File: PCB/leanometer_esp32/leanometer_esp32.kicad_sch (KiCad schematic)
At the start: 32 parts, among them J1 DM3AT-SF-PEJM5, J2 MPU6050, J3 PROG, J4 VBAT, SW1 SW_MEC_5E, SW2 IO0, SW3 EN, U1 ESP32-WROOM-32D, U2 LD1117S33TR_SOT223

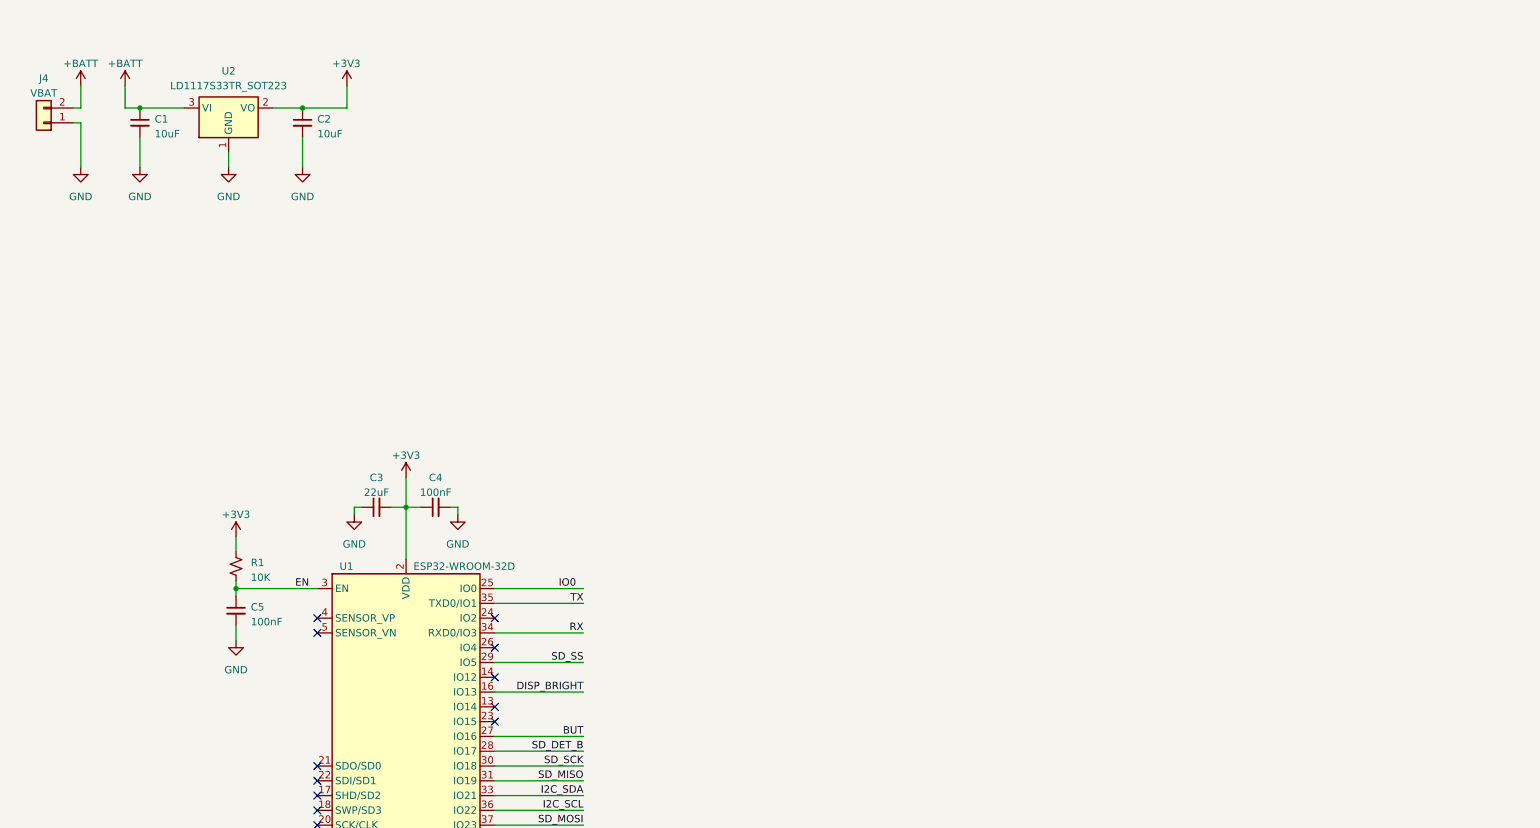
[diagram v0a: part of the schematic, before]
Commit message: Added MPU6050 group
Signed-off-by: theloukou
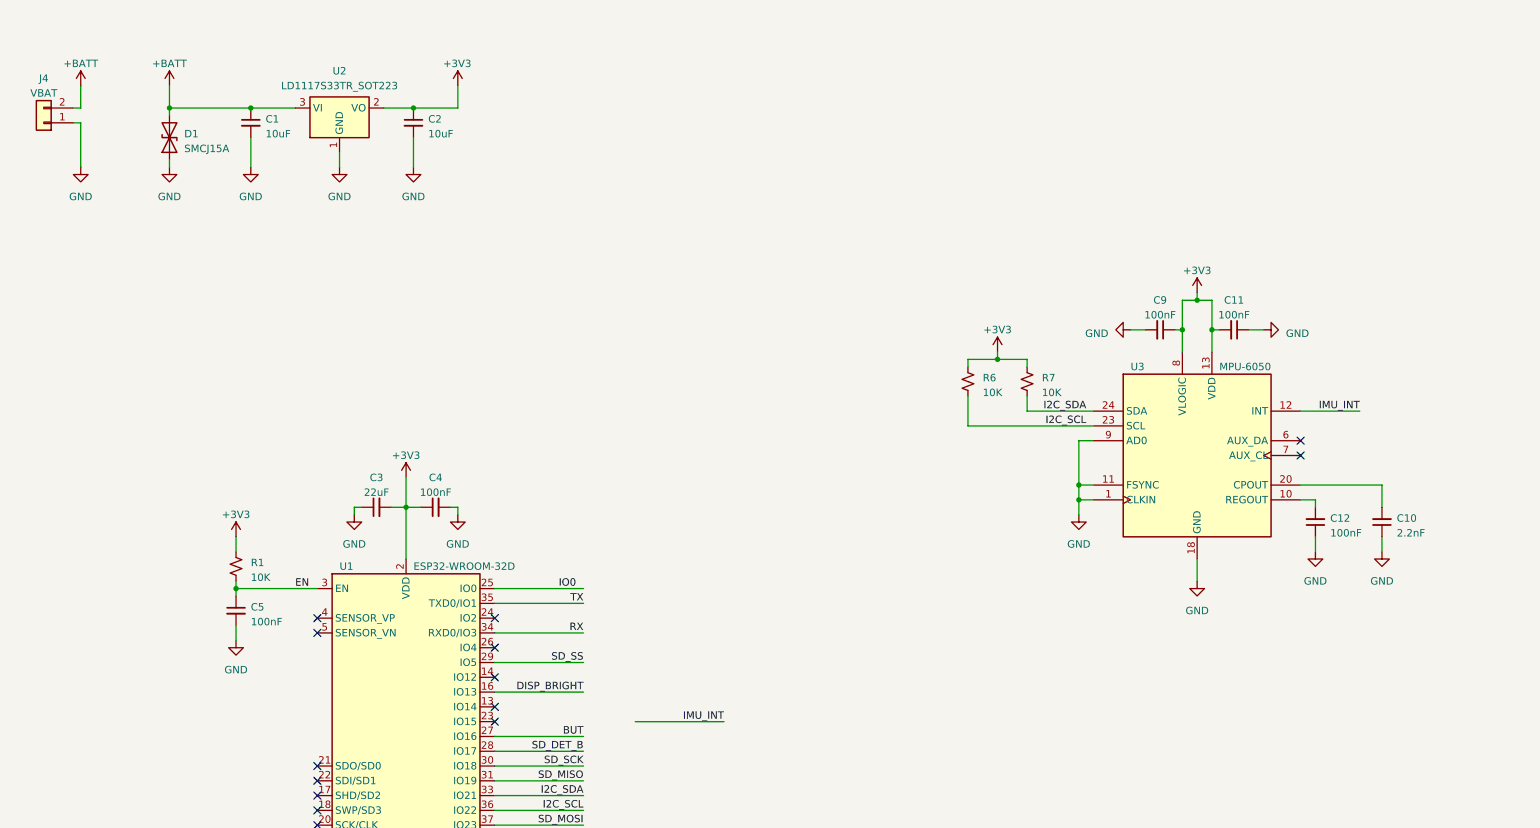
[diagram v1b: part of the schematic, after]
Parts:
- added C10: 2.2nF, symbol Device:C_Small
- added C11, C12, C9: 100nF, symbol Device:C_Small
- added D1: SMCJ15A, Diode_SMD:D_SMC, symbol Device:D_TVS
- added R6, R7: 10K, symbol Device:R_Small_US
- added U3: MPU-6050, Sensor_Motion:InvenSense_QFN-24_4x4mm_P0.5mm, symbol Sensor_Motion:MPU-6050
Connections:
- net +3V3: now also C11.2, C9.1, R6.1, R7.1, U3.13 (VDD), U3.8 (VLOGIC)
- net +BATT: now also D1.2 (A2)
- net GND: now also C10.1, C11.1, C12.1, C9.2, D1.1 (A1), U3.1 (CLKIN), U3.11 (FSYNC), U3.18 (GND), U3.9 (AD0)
- net I2C_SCL: now also R6.2, U3.23 (SCL)
- net I2C_SDA: now also R7.2, U3.24 (SDA)
- new net: C10.2, U3.20 (CPOUT)
- new net: C12.2, U3.10 (REGOUT)
- new net IMU_INT: U3.12 (INT)
- no-connect marks 15 -> 17
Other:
- moved on the sheet: C1, C2, U2

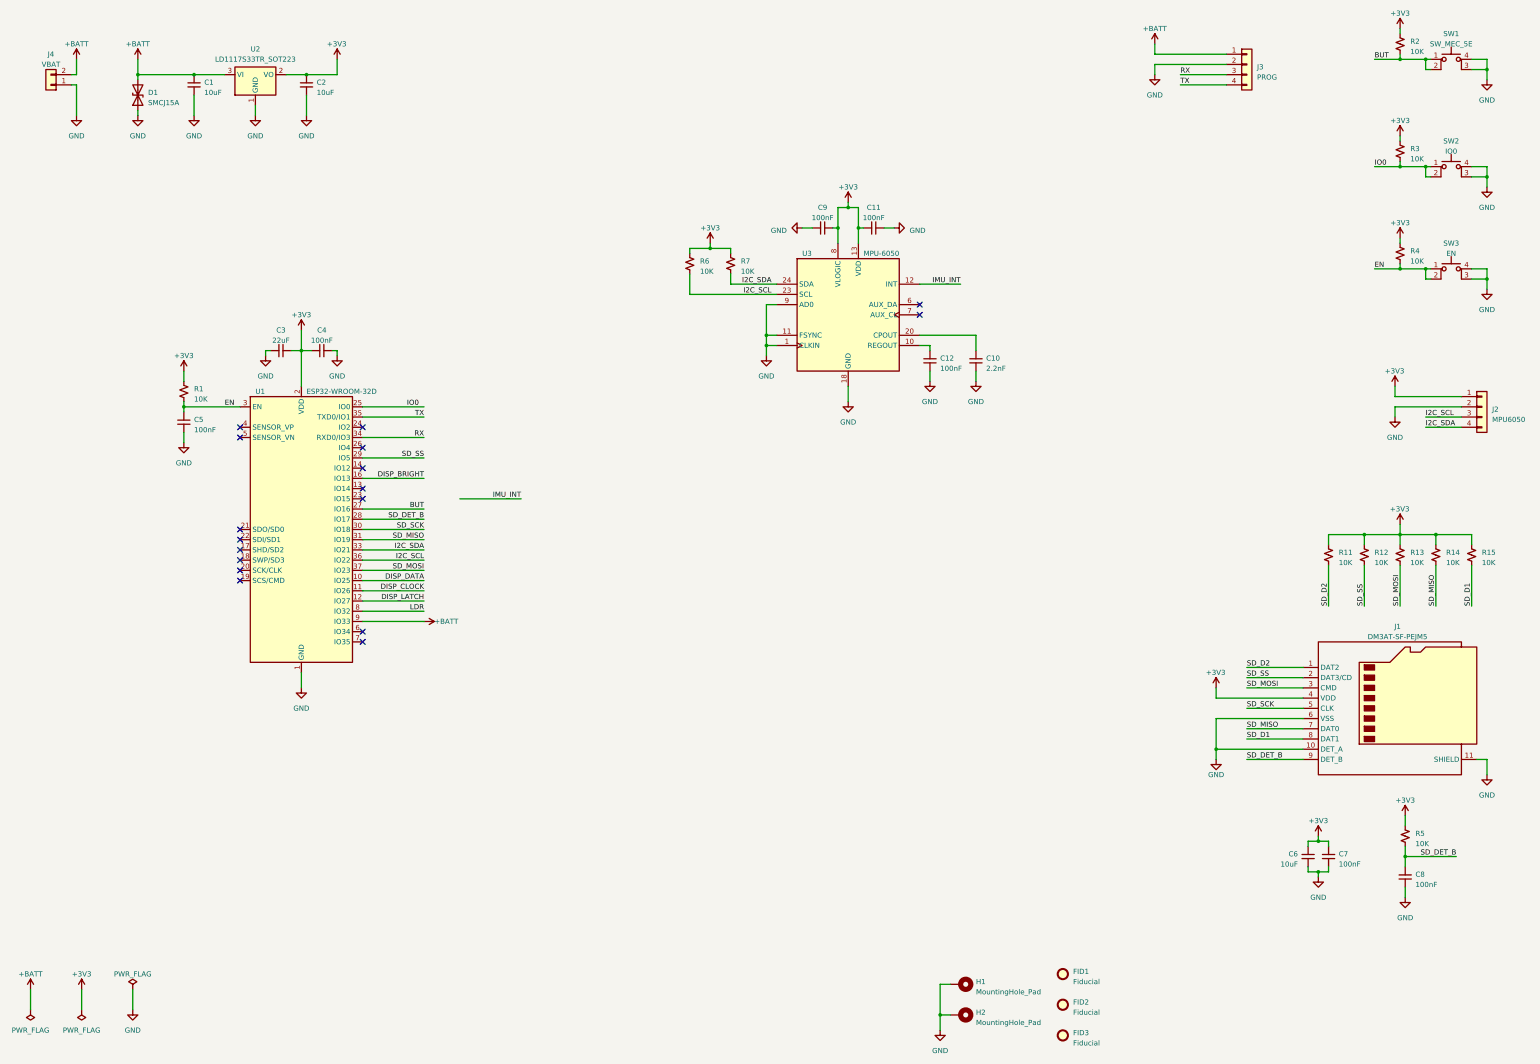
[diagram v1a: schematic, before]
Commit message: Switched schematic to hierarchical layout, rough component placement on layout
Signed-off-by: theloukou
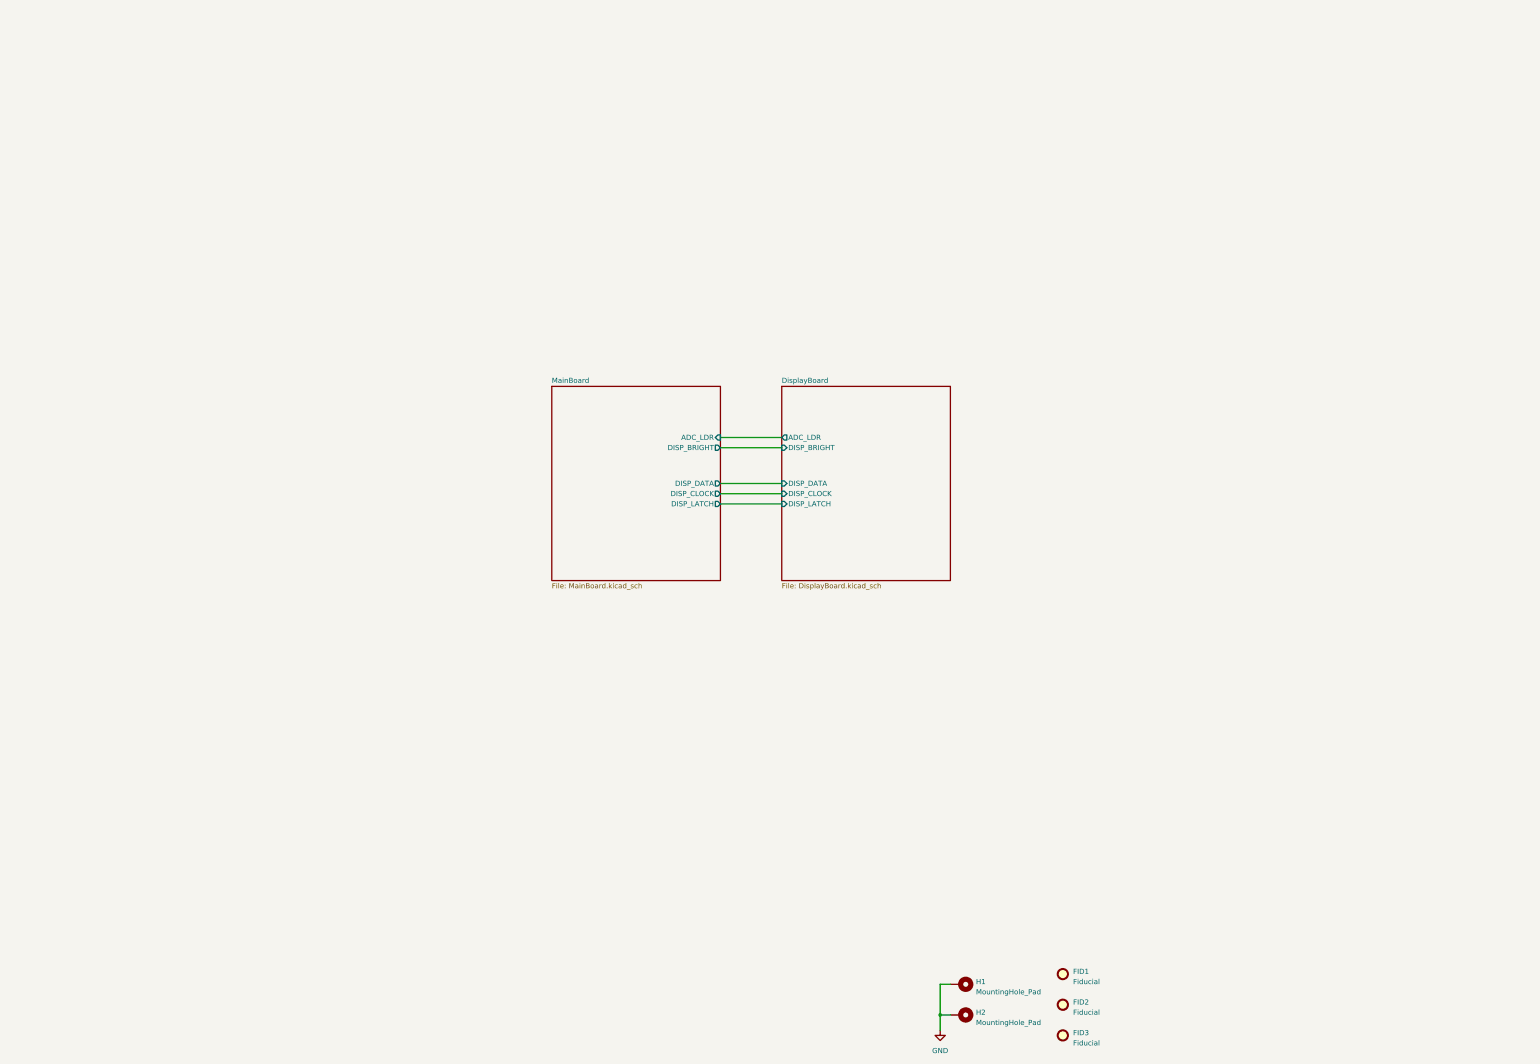
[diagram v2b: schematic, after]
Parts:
- removed C1, C2, C6: 10uF, symbol Device:C_Small
- removed C10: 2.2nF, symbol Device:C_Small
- removed C11, C12, C4, C5, C7, C8, C9: 100nF, symbol Device:C_Small
- removed C3: 22uF, symbol Device:C_Small
- removed D1: SMCJ15A, Diode_SMD:D_SMC, symbol Device:D_TVS
- removed J1: DM3AT-SF-PEJM5, symbol Connector:Micro_SD_Card_Det2
- removed J2: MPU6050, symbol Connector_Generic:Conn_01x04
- removed J3: PROG, symbol Connector_Generic:Conn_01x04
- removed J4: VBAT, symbol Connector_Generic:Conn_01x02
- removed R1, R11, R12, R13, R14, R15, R2, R3, R4, R5, R6, R7: 10K, symbol Device:R_Small_US
- removed SW1: SW_MEC_5E, symbol Switch:SW_MEC_5E
- removed SW2: IO0, symbol Switch:SW_MEC_5E
- removed SW3: EN, symbol Switch:SW_MEC_5E
- removed U1: ESP32-WROOM-32D, RF_Module:ESP32-WROOM-32D, symbol RF_Module:ESP32-WROOM-32D
- removed U2: LD1117S33TR_SOT223, Package_TO_SOT_SMD:SOT-223-3_TabPin2, symbol Regulator_Linear:LD1117S33TR_SOT223
- removed U3: MPU-6050, Sensor_Motion:InvenSense_QFN-24_4x4mm_P0.5mm, symbol Sensor_Motion:MPU-6050
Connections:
- no-connect marks 17 -> 0
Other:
- added sheet DisplayBoard (DisplayBoard.kicad_sch)
- added sheet MainBoard (MainBoard.kicad_sch)
